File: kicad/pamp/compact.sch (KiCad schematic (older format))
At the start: 75 parts, among them J1 Screw_Terminal_01x03, J2 Screw_Terminal_01x02, J3 Screw_Terminal_01x03, Q1 2SA1381F, Q10 BC546B, Q11 2SA1381F, Q12 MJE340, Q13 MJE340, Q14 2SC3503F, Q15 BC546B, Q16 BC556B, Q17 IRFP240N, Q18 IRFP9240N, Q2 2SC3503F, Q3 2SA1381F, Q4 2SC3503F, Q5 BC550C, Q6 BC560C, Q7 BC550C, Q8 BC560C, Q9 BC556B

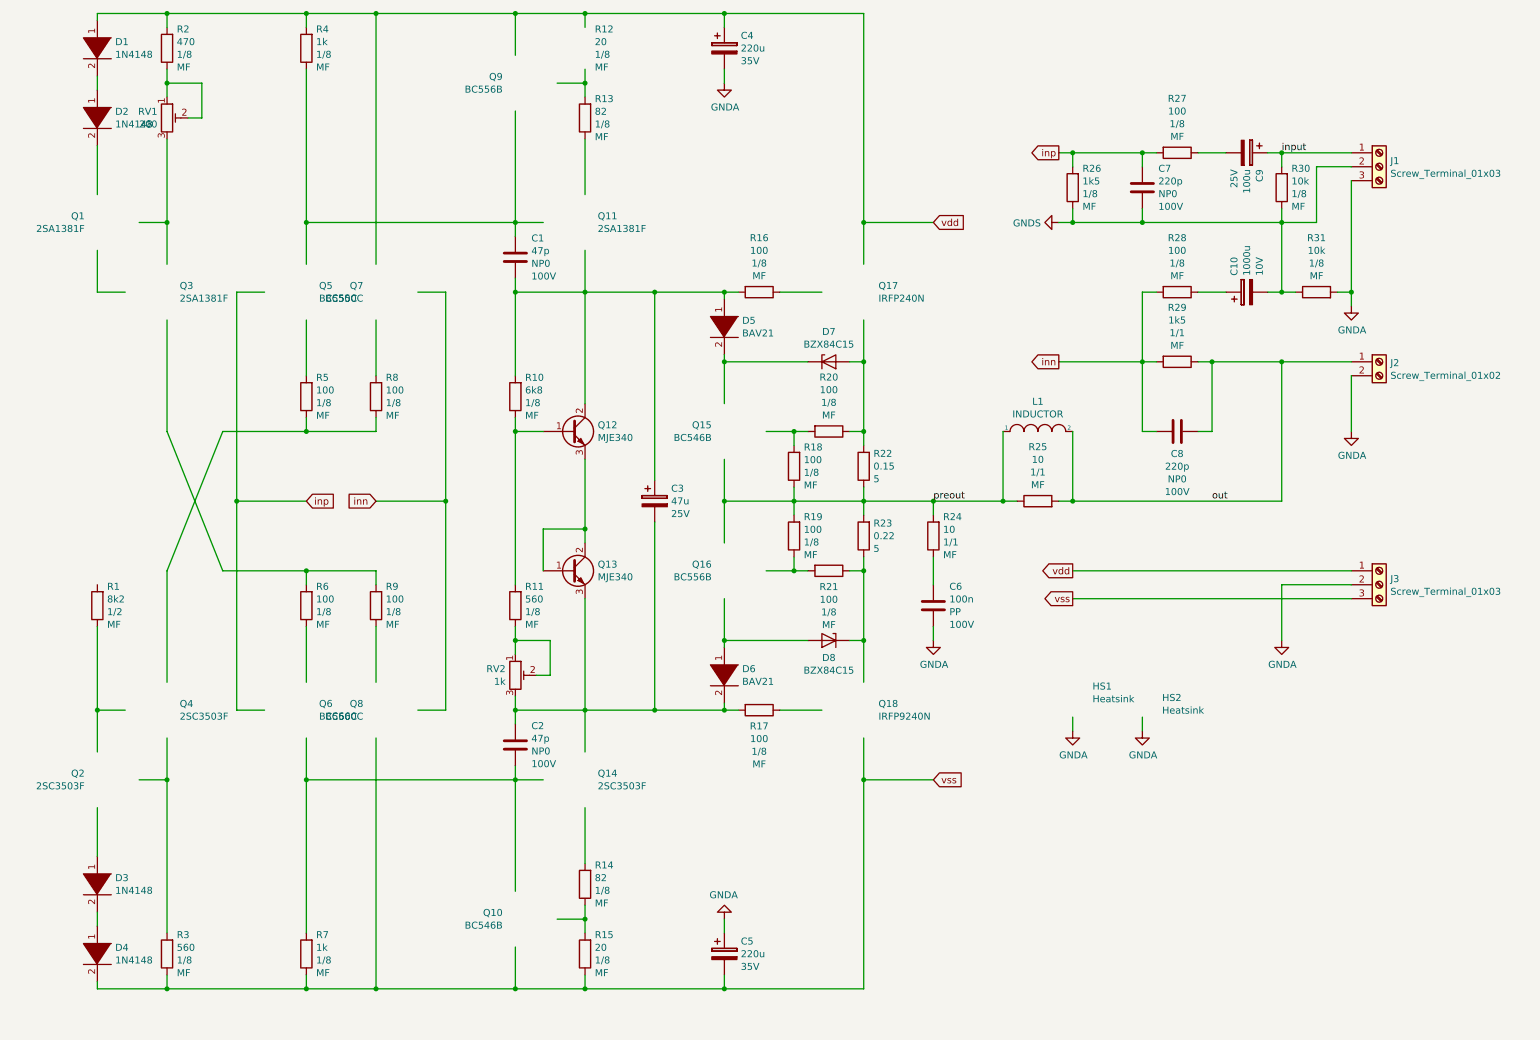
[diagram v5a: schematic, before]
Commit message: Completed schematic and part placement
Signed-off-by: Nenad Radulovic <nenad.b.radulovic@gmail.com>
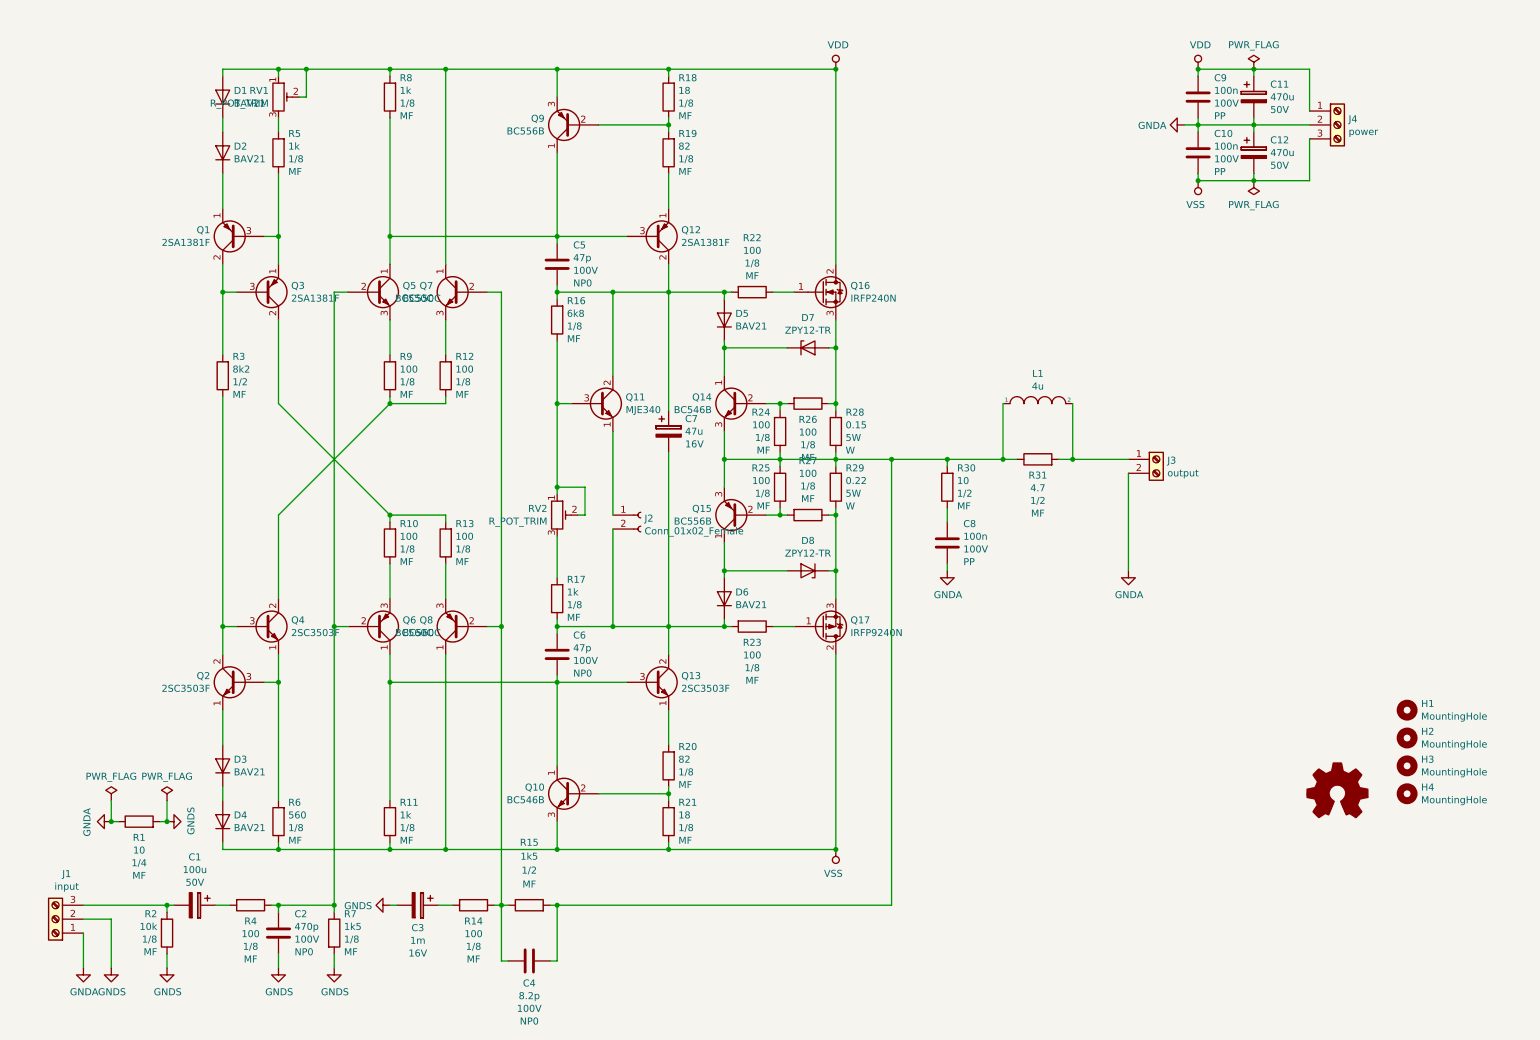
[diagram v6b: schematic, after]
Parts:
- removed C1: 47p, Capacitor_THT:C_Disc_D3.0mm_W2.0mm_P2.50mm, symbol Device:C
- removed C10: 1000u, Capacitor_THT:CP_Radial_D8.0mm_P3.50mm, symbol Device:CP
- removed C4, C5: 220u, Capacitor_THT:CP_Radial_D10.0mm_P3.80mm, symbol Device:CP
- removed C7: 220p, Capacitor_THT:C_Disc_D3.4mm_W2.1mm_P2.50mm, symbol Device:C
- removed C9: 100u, Capacitor_THT:CP_Radial_D8.0mm_P2.50mm, symbol Device:CP
- removed D1, D2, D3, D4: 1N4148, Diode_THT:D_DO-41_SOD81_P7.62mm_Horizontal, symbol pspice:DIODE
- removed D5, D6: BAV21, Diode_THT:D_DO-41_SOD81_P7.62mm_Horizontal, symbol pspice:DIODE
- removed HS1, HS2: Heatsink, Heatsink:Heatsink_Stonecold_HS-132_32x14mm_2xFixation1.5mm, symbol Mechanical:Heatsink_Pad
- removed J2: Screw_Terminal_01x02, TerminalBlock_Phoenix:TerminalBlock_Phoenix_MKDS-1,5-2_1x02_P5.00mm_Horizontal, symbol Connector:Screw_Terminal_01x02
- removed J3: Screw_Terminal_01x03, TerminalBlock_Phoenix:TerminalBlock_Phoenix_MKDS-1,5-3_1x03_P5.00mm_Horizontal, symbol Connector:Screw_Terminal_01x03
- removed Q11: 2SA1381F, Package_TO_SOT_THT:TO-126-3_Vertical, symbol Device:Q_PNP_ECB
- removed Q12, Q13: MJE340, Package_TO_SOT_THT:TO-126-3_Vertical, symbol Device:Q_NPN_BCE
- removed Q14: 2SC3503F, Package_TO_SOT_THT:TO-126-3_Vertical, symbol Device:Q_NPN_ECB
- removed Q15: BC546B, Package_TO_SOT_THT:TO-92L_Inline, symbol Device:Q_NPN_CBE
- removed Q16: BC556B, Package_TO_SOT_THT:TO-92L_Inline, symbol Device:Q_PNP_CBE
- removed Q17: IRFP240N, Package_TO_SOT_THT:TO-247-3_Vertical, symbol Transistor_FET:IRF540N
- removed Q18: IRFP9240N, Package_TO_SOT_THT:TO-247-3_Vertical, symbol Transistor_FET:IRF9540N
- added C1: 100u, Capacitor_THT:CP_Radial_D10.0mm_P3.50mm, symbol Device:CP
- added C10, C9: 100n, Capacitor_THT:C_Rect_L7.2mm_W5.5mm_P5.00mm_FKS2_FKP2_MKS2_MKP2, symbol Device:C
- added C11, C12: 470u, Capacitor_THT:CP_Radial_D10.0mm_P3.50mm, symbol Device:CP
- added C4: 8.2p, Capacitor_THT:C_Disc_D3.0mm_W2.0mm_P2.50mm, symbol Device:C
- added C5: 47p, Capacitor_THT:C_Disc_D3.0mm_W2.0mm_P2.50mm, symbol Device:C
- added C7: 47u, Capacitor_THT:CP_Radial_D8.0mm_P2.50mm, symbol Device:CP
- added D1, D2, D3, D4, D5, D6: BAV21, Diode_THT:D_DO-41_SOD81_P7.62mm_Horizontal, symbol Device:D
- added H1, H2, H3, H4: MountingHole, MountingHole:MountingHole_3.2mm_M3_Pad, symbol Mechanical:MountingHole
- added J2: Conn_01x02_Female, Connector_PinHeader_2.54mm:PinHeader_1x02_P2.54mm_Vertical, symbol Connector:Conn_01x02_Female
- added J3: output, TerminalBlock_Phoenix:TerminalBlock_Phoenix_MKDS-1,5-2_1x02_P5.00mm_Horizontal, symbol Connector:Screw_Terminal_01x02
- added J4: power, TerminalBlock_Phoenix:TerminalBlock_Phoenix_MKDS-1,5-3-5.08_1x03_P5.08mm_Horizontal, symbol Connector:Screw_Terminal_01x03
- added Q11: MJE340, Package_TO_SOT_THT:TO-126-3_Vertical, symbol Device:Q_NPN_ECB
- added Q12: 2SA1381F, Package_TO_SOT_THT:TO-126-3_Vertical, symbol Device:Q_PNP_ECB
- added Q13: 2SC3503F, Package_TO_SOT_THT:TO-126-3_Vertical, symbol Device:Q_NPN_ECB
- added Q14: BC546B, Package_TO_SOT_THT:TO-92L_Inline, symbol Device:Q_NPN_CBE
- added Q15: BC556B, Package_TO_SOT_THT:TO-92L_Inline, symbol Device:Q_PNP_CBE
- added Q16: IRFP240N, Package_TO_SOT_THT:TO-247-3_Vertical, symbol Transistor_FET:IRF540N
- added Q17: IRFP9240N, Package_TO_SOT_THT:TO-247-3_Vertical, symbol Transistor_FET:IRF9540N
- C2: value 47p -> 470p; footprint Capacitor_THT:C_Disc_D3.0mm_W2.0mm_P2.50mm -> Capacitor_THT:C_Disc_D3.8mm_W2.6mm_P2.50mm
- C3: value 47u -> 1m; footprint Capacitor_THT:CP_Radial_D6.3mm_P2.50mm -> Capacitor_THT:CP_Radial_D10.0mm_P3.50mm; Voltage 25V -> 16V
- C6: value 100n -> 47p; footprint Capacitor_THT:C_Rect_L7.2mm_W3.5mm_P5.00mm_FKS2_FKP2_MKS2_MKP2 -> Capacitor_THT:C_Disc_D3.0mm_W2.0mm_P2.50mm; Type PP -> NP0
- C8: value 220p -> 100n; footprint Capacitor_THT:C_Disc_D3.4mm_W2.1mm_P2.50mm -> Capacitor_THT:C_Rect_L7.2mm_W5.5mm_P5.00mm_FKS2_FKP2_MKS2_MKP2; Type NP0 -> PP
- D7, D8: value BZX84C15 -> ZPY12-TR
- J1: value Screw_Terminal_01x03 -> input; footprint TerminalBlock_Phoenix:TerminalBlock_Phoenix_MKDS-1,5-3_1x03_P5.00mm_Horizontal -> TerminalBlock_Phoenix:TerminalBlock_Phoenix_PT-1,5-3-3.5-H_1x03_P3.50mm_Horizontal
- L1: value INDUCTOR -> 4u; footprint Inductor_THT:L_Axial_L26.7mm_D14.0mm_P7.62mm_Vertical_Vishay_IHA-104 -> Inductor_THT:L_Axial_L29.9mm_D14.0mm_P7.62mm_Vertical_Vishay_IHA-105
- R1: value 8k2 -> 10; Power 1/2 -> 1/4
- R10: value 6k8 -> 100
- R11: value 560 -> 1k
- R12: value 20 -> 100
- R13, R14: value 82 -> 100
- R15: value 20 -> 1k5; footprint Resistor_THT:R_Axial_DIN0207_L6.3mm_D2.5mm_P10.16mm_Horizontal -> Resistor_THT:R_Axial_DIN0411_L9.9mm_D3.6mm_P12.70mm_Horizontal; Power 1/8 -> 1/2
- R16: value 100 -> 6k8
- R17, R5, R8: value 100 -> 1k
- R18, R21: value 100 -> 18
- R19, R20: value 100 -> 82
- R2: value 470 -> 10k
- R22: value 0.15 -> 100; Power 5 -> 1/8; Type (none) -> MF
- R23: value 0.22 -> 100; Power 5 -> 1/8; Type (none) -> MF
- R24, R25: value 10 -> 100; Power 1/1 -> 1/8
- R26: value 1k5 -> 100
- R28: value 100 -> 0.15; footprint Resistor_THT:R_Axial_DIN0207_L6.3mm_D2.5mm_P10.16mm_Horizontal -> Resistor_THT:R_Box_L14.0mm_W5.0mm_P9.00mm; Power 1/8 -> 5W; Type MF -> W
- R29: value 1k5 -> 0.22; footprint Resistor_THT:R_Axial_DIN0207_L6.3mm_D2.5mm_P10.16mm_Horizontal -> Resistor_THT:R_Box_L14.0mm_W5.0mm_P9.00mm; Power 1/1 -> 5W; Type MF -> W
- R3: value 560 -> 8k2; footprint Resistor_THT:R_Axial_DIN0207_L6.3mm_D2.5mm_P10.16mm_Horizontal -> Resistor_THT:R_Axial_DIN0411_L9.9mm_D3.6mm_P12.70mm_Horizontal; Power 1/8 -> 1/2
- R30: value 10k -> 10; footprint Resistor_THT:R_Axial_DIN0207_L6.3mm_D2.5mm_P10.16mm_Horizontal -> Resistor_THT:R_Axial_DIN0411_L9.9mm_D3.6mm_P12.70mm_Horizontal; Power 1/8 -> 1/2
- R31: value 10k -> 4.7; footprint Resistor_THT:R_Axial_DIN0207_L6.3mm_D2.5mm_P10.16mm_Horizontal -> Resistor_THT:R_Axial_DIN0411_L9.9mm_D3.6mm_P12.70mm_Horizontal; Power 1/8 -> 1/2
- R4: value 1k -> 100
- R6: value 100 -> 560
- R7: value 1k -> 1k5
- RV1: value 200 -> R_POT_TRIM
- RV2: value 1k -> R_POT_TRIM
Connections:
- net labels added: VDD, VSS
- net labels removed: inn, inp, input, out, preout, vdd, vss
- wire segments 220 -> 207

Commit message: WIP: Done schematic.
Signed-off-by: Nenad Radulovic <nenad.b.radulovic@gmail.com>
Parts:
- removed C5, C6: 47p, Capacitor_THT:C_Disc_D3.0mm_W2.0mm_P2.50mm, symbol Device:C
- removed C7: 47u, Capacitor_THT:CP_Radial_D8.0mm_P2.50mm, symbol Device:CP
- removed D1, D2, D3, D4: BAV21, Diode_THT:D_DO-41_SOD81_P7.62mm_Horizontal, symbol Device:D
- removed D7, D8: ZPY12-TR, Diode_THT:D_DO-41_SOD81_P10.16mm_Horizontal, symbol Device:D_Zener
- removed J2: Conn_01x02_Female, Connector_PinHeader_2.54mm:PinHeader_1x02_P2.54mm_Vertical, symbol Connector:Conn_01x02_Female
- removed Q1: 2SA1381F, Package_TO_SOT_THT:TO-126-3_Vertical, symbol Device:Q_PNP_ECB
- removed Q16: IRFP240N, Package_TO_SOT_THT:TO-247-3_Vertical, symbol Transistor_FET:IRF540N
- removed Q17: IRFP9240N, Package_TO_SOT_THT:TO-247-3_Vertical, symbol Transistor_FET:IRF9540N
- removed Q2, Q4: 2SC3503F, Package_TO_SOT_THT:TO-126-3_Vertical, symbol Device:Q_NPN_ECB
- removed Q5, Q7: BC550C, Package_TO_SOT_THT:TO-92L_Inline, symbol Device:Q_NPN_CBE
- removed R12, R25, R27, R9: 100, Resistor_THT:R_Axial_DIN0207_L6.3mm_D2.5mm_P10.16mm_Horizontal, symbol Device:R
- removed R19: 82, Resistor_THT:R_Axial_DIN0207_L6.3mm_D2.5mm_P10.16mm_Horizontal, symbol Device:R
- removed R6: 560, Resistor_THT:R_Axial_DIN0207_L6.3mm_D2.5mm_P10.16mm_Horizontal, symbol Device:R
- removed R8: 1k, Resistor_THT:R_Axial_DIN0207_L6.3mm_D2.5mm_P10.16mm_Horizontal, symbol Device:R
- removed RV1: R_POT_TRIM, Potentiometer_THT:Potentiometer_ACP_CA9-V10_Vertical, symbol Device:R_POT_TRIM
- added C? (x3): 100p, Capacitor_THT:C_Disc_D8.0mm_W2.5mm_P5.00mm, symbol Device:C
- added C? (x2): 4u7, Capacitor_THT:CP_Radial_D5.0mm_P2.50mm, symbol Device:CP
- added C? (x2): 100n, Capacitor_THT:C_Rect_L7.2mm_W2.5mm_P5.00mm_FKS2_FKP2_MKS2_MKP2, symbol Device:C
- added C?: 220n, Capacitor_THT:C_Rect_L7.2mm_W4.5mm_P5.00mm_FKS2_FKP2_MKS2_MKP2, symbol Device:C
- added C?: 1n, Capacitor_THT:C_Disc_D8.0mm_W2.5mm_P5.00mm, symbol Device:C
- added D? (x2): BZX84B22VL, Diode_THT:D_DO-41_SOD81_P7.62mm_Horizontal, symbol Device:D_Zener
- added D?: BAV21, Diode_THT:D_DO-41_SOD81_P7.62mm_Horizontal, symbol Device:D
- added Q?: 2SC4793, Package_TO_SOT_THT:TO-220-3_Vertical, symbol Device:Q_NPN_BCE
- added Q? (x2): Q_PNP_BCE, symbol Device:Q_PNP_BCE
- added Q?: BC556B, Package_TO_SOT_THT:TO-92L_Inline, symbol Device:Q_PNP_CBE
- added Q? (x2): BC550C, Package_TO_SOT_THT:TO-92L_Inline, symbol Device:Q_NPN_CBE
- added Q?: BC546B, Package_TO_SOT_THT:TO-92L_Inline, symbol Device:Q_NPN_CBE
- added Q?: MJL3281, Package_TO_SOT_THT:TO-220-3_Vertical, symbol Device:Q_NPN_BCE
- added R? (x3): 220, Resistor_THT:R_Axial_DIN0207_L6.3mm_D2.5mm_P10.16mm_Horizontal, symbol Device:R
- added R? (x2): 10, Resistor_THT:R_Axial_DIN0207_L6.3mm_D2.5mm_P10.16mm_Horizontal, symbol Device:R
- added R?: 120, Resistor_THT:R_Axial_DIN0207_L6.3mm_D2.5mm_P10.16mm_Horizontal, symbol Device:R
- added R?: 51, Resistor_THT:R_Axial_DIN0207_L6.3mm_D2.5mm_P10.16mm_Horizontal, symbol Device:R
- added R? (x4): 1k, Resistor_THT:R_Axial_DIN0207_L6.3mm_D2.5mm_P10.16mm_Horizontal, symbol Device:R
- added R? (x4): 10k, Resistor_THT:R_Axial_DIN0207_L6.3mm_D2.5mm_P10.16mm_Horizontal, symbol Device:R
- added R? (x2): 3k6, Resistor_THT:R_Axial_DIN0207_L6.3mm_D2.5mm_P10.16mm_Horizontal, symbol Device:R
- added R?: 620, Resistor_THT:R_Axial_DIN0207_L6.3mm_D2.5mm_P10.16mm_Horizontal, symbol Device:R
- added R?: 6k2, Resistor_THT:R_Axial_DIN0411_L9.9mm_D3.6mm_P12.70mm_Horizontal, symbol Device:R
- added R?: 33, Resistor_THT:R_Axial_DIN0207_L6.3mm_D2.5mm_P10.16mm_Horizontal, symbol Device:R
- added R? (x2): 510, Resistor_THT:R_Axial_DIN0207_L6.3mm_D2.5mm_P10.16mm_Horizontal, symbol Device:R
- added R?: 910, Resistor_THT:R_Axial_DIN0207_L6.3mm_D2.5mm_P10.16mm_Horizontal, symbol Device:R
- added R? (x2): 2R2, Resistor_THT:R_Axial_DIN0207_L6.3mm_D2.5mm_P10.16mm_Horizontal, symbol Device:R
- R10, R13: value 100 -> 220
- R11, R5: value 1k -> 120
- R16: value 6k8 -> 1k
- R17: value 1k -> 220
- R18: value 18 -> 33
- R20: value 82 -> 2
- R22, R23: value 100 -> 22
- R24: value 100 -> 33
- R26: value 100 -> 910
- R28: value 0.15 -> 0.22
- R3: value 8k2 -> 6k2
- RV2: value R_POT_TRIM -> 1k
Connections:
- net GNDA: now also R3.1, Q?.1 (C), R?.1, R?.2
- net VDD: now also R5.2, Q?.2 (C), Q?.2 (C), Q?.3 (E), R?.2
- net VSS: now also C?.2, Q?.2 (C), Q?.2 (C), R?.1, R?.1, R?.1; no longer Q8.1 (C)
- net at R22.1: now also Q?.1 (B)
- net at R26.1, R28.2: now also Q?.3 (E)
- net at D5.2 (A), Q11.2 (C), R22.2: now also C?.1, R?.1; no longer Q12.2 (C), R16.2
- net at L1.1, Q14.3 (E), Q15.3 (E)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: now also C?.1, C?.2, R?.1, R?.1, R?.2, R?.2, R?.2, R?.2; no longer C4.1, R15.2, R29.2
- net at R29.1: now also Q?.3 (E), R?.1
- net at R23.1: now also Q?.1 (B)
- net at D6.1 (K), Q13.2 (C), R17.1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: now also Q11.1 (E), C?.1, C?.2, D?.1 (K)
- net at Q14.2 (B), R26.2: now also C?.1, R?.1, R?.2; no longer R24.2
- net at Q15.2 (B): now also C?.2, R?.1, R?.2, R?.2
- net at Q10.1 (C), Q6.1 (C): now also D?.2 (A), Q?.1 (C), Q?.2 (B), R?.1; no longer Q13.3 (B), R11.2
- net at R20.1, R21.2: now also R?.1; no longer Q10.2 (B)
- net at Q12.1 (E): now also R18.1, R?.2
- net at Q12.3 (B), Q9.1 (C): now also R?.2
- net at Q9.2 (B): now also R?.1; no longer R18.1
- net at C4.2, R14.1, R15.1: no longer Q8.2 (B)
- net at C2.2, R4.1, R7.1: no longer Q6.2 (B)
- net at Q3.1 (E), R5.1: now also R?.1
- net at Q3.3 (B), R3.2: now also Q?.1 (C)
- new net: C?.2, R24.2
- new net: Q12.2 (C), R16.2, R?.2
- new net: Q13.3 (B), Q?.3 (E), R?.2
- new net: Q10.2 (B), R?.2
- new net: Q8.1 (C), Q?.1 (C), Q?.2 (B), Q?.2 (B)
- new net: C?.1, Q?.3 (E), R11.2
- new net: Q?.3 (E), R?.2, R?.2
- new net: Q?.3 (E), R?.1, R?.2
- new net: Q?.2 (B), R?.2
- new net: C?.2, Q?.3 (E), R?.2
- new net: C?.1, R?.1 (x2)
- new net: C?.1, R?.1, R?.2
- new net: D?.1 (K), R?.1, R?.2
- new net: C?.1, C?.2, R?.1
- new net: C?.2, R?.2
- new net: C4.1, R15.2
- new net: D?.2 (A), R?.2
- new net: D?.1 (K), R?.1
- new net: D?.2 (A), R?.1, R?.2
- new net: C?.2, R?.1, R?.2
- new net: Q?.1 (B), R?.1 (x2)
- new net inv: Q8.2 (B)
- new net ninv: Q6.2 (B)
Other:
- moved on the sheet: C1, C2, C3, C4, C8, D5, D6, J1, J3, L1, Q10, Q11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
